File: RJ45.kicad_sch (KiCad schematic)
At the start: 13 parts, among them J1 0826-1X1T-JK-F, U1 KSZ8081MLX, U8 OSC_25M

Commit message: Routing changes, pullups, etc
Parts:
- C1, C2, C3, C34, C35, C36, C4, J1, R1, R23, R24, U1: Source (none) -> ANY
- U8: value OSC_25M -> ASEMB-25.000MHZ-LC-T; Source (none) -> ANY

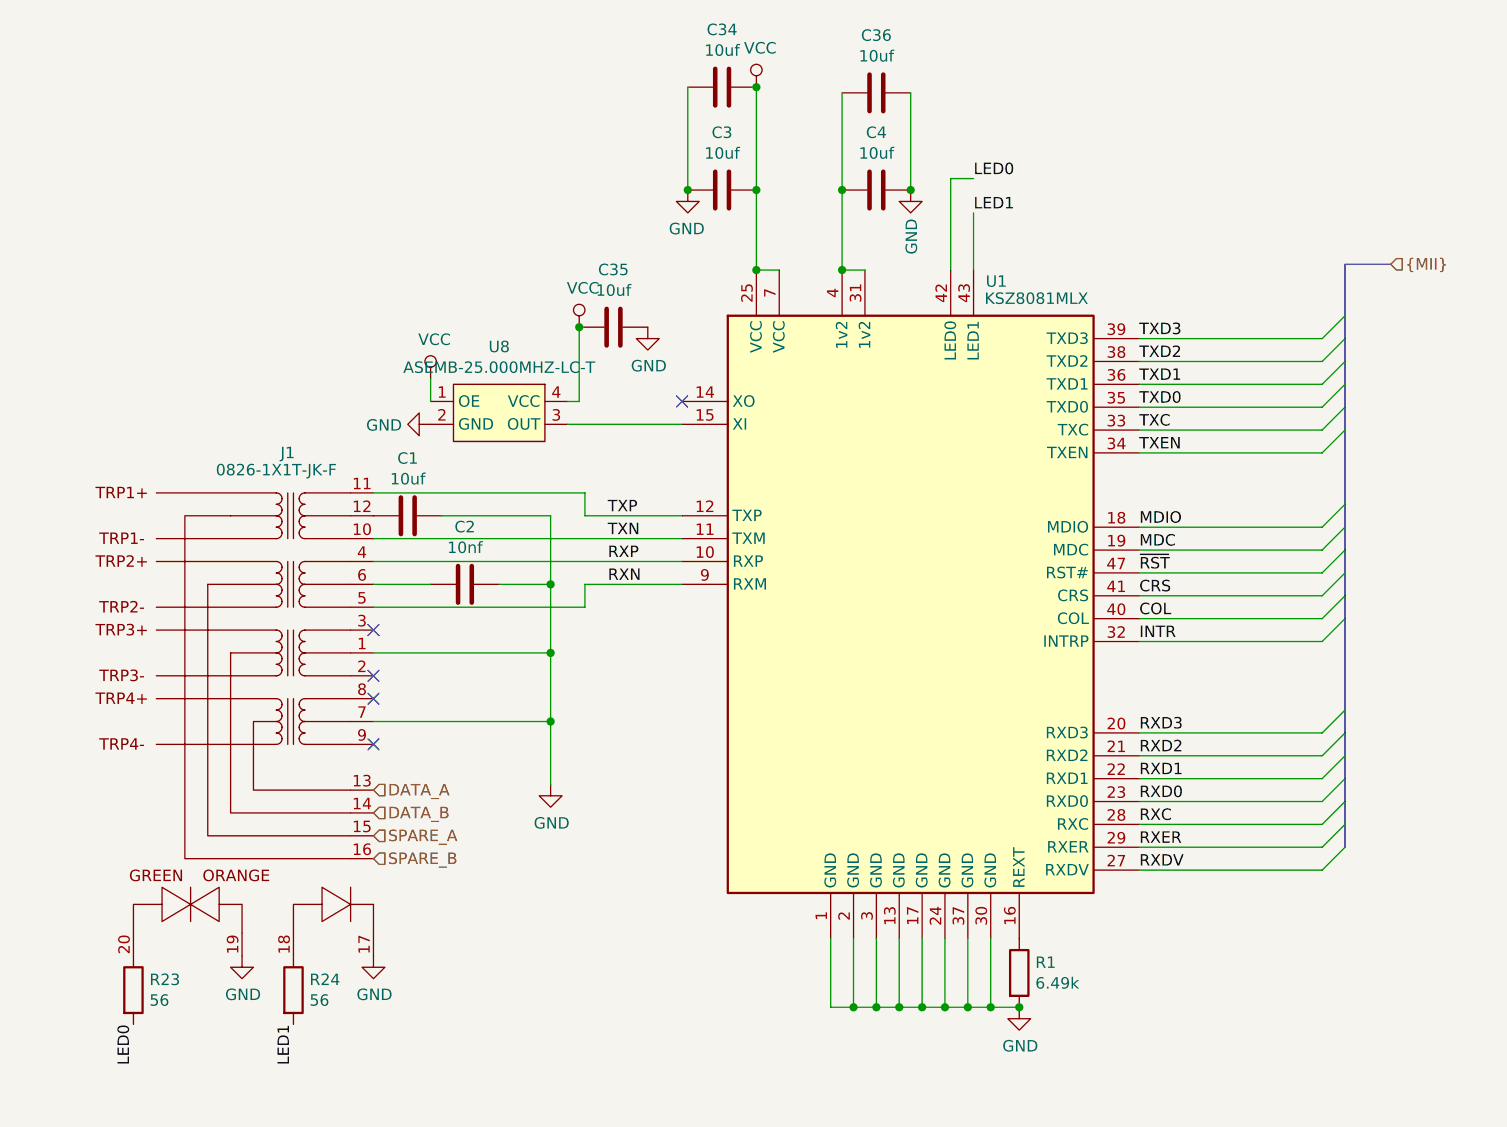
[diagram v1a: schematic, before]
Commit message: Routing cleanup, fix primary transformer
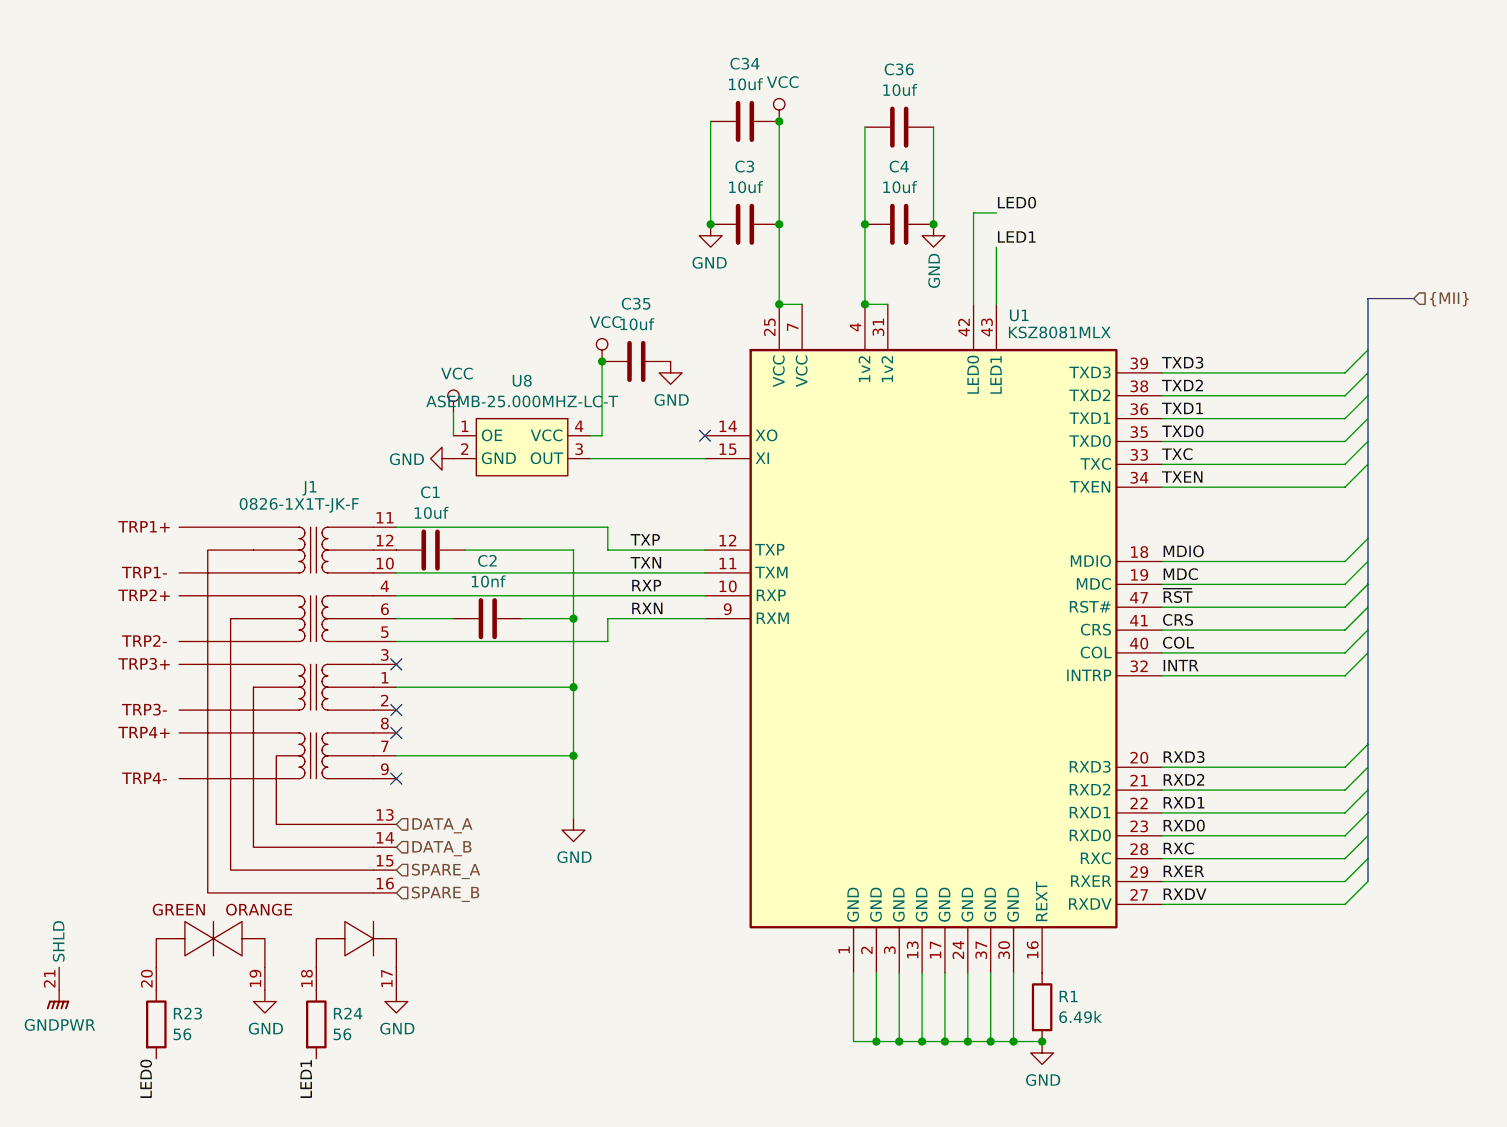
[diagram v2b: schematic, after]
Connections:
- new net GNDPWR: J1.21 (SHLD), J1.22 (SHLD)
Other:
- moved on the sheet: C1, C2, C3, C34, C35, C36, C4, R1, R23, R24, U1, U8

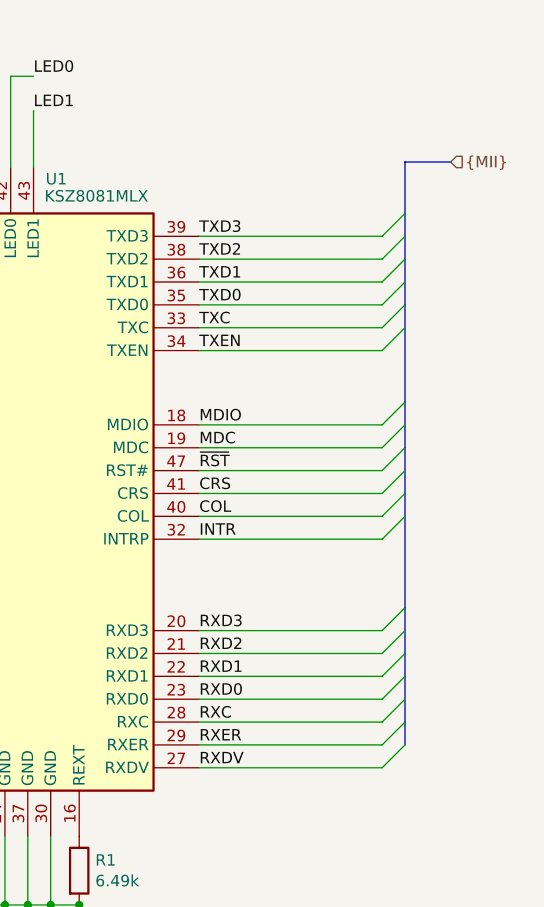
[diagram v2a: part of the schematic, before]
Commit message: Change PoE controller to NCP1081
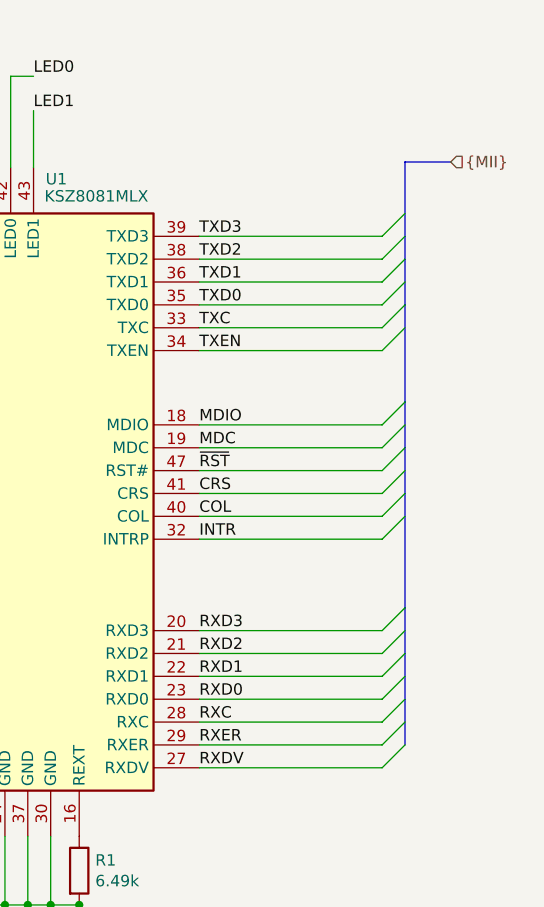
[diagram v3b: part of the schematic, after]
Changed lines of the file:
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@@
-(kicad_sch (version 20200512) (host eeschema "5.99.0-unknown-eae0c14~101~ubuntu20.04.1")
+(kicad_sch (version 20200608) (host eeschema "5.99.0-unknown-8bd9b26~101~ubuntu20.04.1")
   (page 2 7)
   (paper "A4")
@@
   (junction (at 177.8 137.795))
   (junction (at 180.975 137.795))
-  (no_connect (at 109.22 95.885))
   (no_connect (at 109.22 103.505))
   (no_connect (at 109.22 100.965))
+  (no_connect (at 109.22 108.585))
   (no_connect (at 143.51 70.485))
-  (no_connect (at 109.22 108.585))
+  (no_connect (at 109.22 95.885))
   (bus_entry (at 214.63 63.5) (size 2.54 -2.54))
   (bus_entry (at 214.63 66.04) (size 2.54 -2.54))
@@
     (stroke (width 0) (type solid) (color 0 0 0 0))
   )
-  (bus (pts (xy 217.17 55.245) (xy 217.17 60.96))
+  (bus (pts (xy 217.17 55.245) (xy 217.17 63.5))
     (stroke (width 0) (type solid) (color 0 0 0 0))
   )
@@
     (stroke (width 0) (type solid) (color 0 0 0 0))
   )
-  (bus (pts (xy 217.17 60.96) (xy 217.17 66.04))
+  (bus (pts (xy 217.17 63.5) (xy 217.17 66.04))
     (stroke (width 0) (type solid) (color 0 0 0 0))
   )
@@
     (stroke (width 0) (type solid) (color 0 0 0 0))
   )
-  (bus (pts (xy 217.17 109.855) (xy 217.17 112.395))
-    (stroke (width 0) (type solid) (color 0 0 0 0))
-  )
-  (bus (pts (xy 217.17 112.395) (xy 217.17 117.475))
-    (stroke (width 0) (type solid) (color 0 0 0 0))
-  )
-  (bus (pts (xy 217.17 117.475) (xy 217.17 120.015))
+  (bus (pts (xy 217.17 109.855) (xy 217.17 114.935))
+    (stroke (width 0) (type solid) (color 0 0 0 0))
+  )
+  (bus (pts (xy 217.17 114.935) (xy 217.17 120.015))
     (stroke (width 0) (type solid) (color 0 0 0 0))
   )
@@
   )
   (symbol (lib_id "power:VCC") (at 115.57 67.945 0) (unit 1)
+    (in_bom yes) (on_board yes)
     (property "Reference" "#PWR0170" (id 0) (at 115.57 71.755 0)
       (effects (font (size 1.27 1.27)) hide)
@@
   )
   (symbol (lib_id "power:VCC") (at 132.08 62.23 0) (unit 1)
+    (in_bom yes) (on_board yes)
     (property "Reference" "#PWR0171" (id 0) (at 132.08 66.04 0)
       (effects (font (size 1.27 1.27)) hide)
@@
   )
   (symbol (lib_id "power:VCC") (at 151.765 35.56 0) (unit 1)
+    (in_bom yes) (on_board yes)
     (property "Reference" "#PWR0102" (id 0) (at 151.765 39.37 0)
       (effects (font (size 1.27 1.27)) hide)
@@
   )
   (symbol (lib_id "power:GNDPWR") (at 71.755 132.08 0) (unit 1)
+    (in_bom yes) (on_board yes)
     (property "Reference" "#PWR0182" (id 0) (at 71.755 137.16 0)
       (effects (font (size 1.27 1.27)) hide)
@@
   )
   (symbol (lib_id "power:GND") (at 94.615 132.08 0) (unit 1)
+    (in_bom yes) (on_board yes)
     (property "Reference" "#PWR0175" (id 0) (at 94.615 138.43 0)
       (effects (font (size 1.27 1.27)) hide)
@@
   )
   (symbol (lib_id "power:GND") (at 109.22 132.08 0) (unit 1)
+    (in_bom yes) (on_board yes)
     (property "Reference" "#PWR0174" (id 0) (at 109.22 138.43 0)
       (effects (font (size 1.27 1.27)) hide)
@@
   )
   (symbol (lib_id "power:GND") (at 115.57 73.025 270) (unit 1)
+    (in_bom yes) (on_board yes)
     (property "Reference" "#PWR0172" (id 0) (at 109.22 73.025 0)
       (effects (font (size 1.27 1.27)) hide)
@@
   )
   (symbol (lib_id "power:GND") (at 128.905 113.03 0) (unit 1)
+    (in_bom yes) (on_board yes)
     (property "Reference" "#PWR0105" (id 0) (at 128.905 119.38 0)
       (effects (font (size 1.27 1.27)) hide)
@@
   )
   (symbol (lib_id "power:GND") (at 139.7 62.23 0) (unit 1)
+    (in_bom yes) (on_board yes)
     (property "Reference" "#PWR0173" (id 0) (at 139.7 68.58 0)
       (effects (font (size 1.27 1.27)) hide)
@@
   )
   (symbol (lib_id "power:GND") (at 144.145 46.99 0) (mirror y) (unit 1)
+    (in_bom yes) (on_board yes)
     (property "Reference" "#PWR0103" (id 0) (at 144.145 53.34 0)
       (effects (font (size 1.27 1.27)) hide)
@@
   )
   (symbol (lib_id "power:GND") (at 168.91 46.99 0) (unit 1)
+    (in_bom yes) (on_board yes)
     (property "Reference" "#PWR0104" (id 0) (at 168.91 53.34 0)
       (effects (font (size 1.27 1.27)) hide)
@@
   )
   (symbol (lib_id "power:GND") (at 180.975 137.795 0) (unit 1)
+    (in_bom yes) (on_board yes)
     (property "Reference" "#PWR0101" (id 0) (at 180.975 144.145 0)
       (effects (font (size 1.27 1.27)) hide)
@@
   )
   (symbol (lib_name "Device:R_1") (lib_id "Device:R") (at 82.55 135.89 0) (unit 1)
+    (in_bom yes) (on_board yes)
     (property "Reference" "R23" (id 0) (at 84.3281 134.7406 0)
       (effects (font (size 1.27 1.27)) (justify left))
@@
   )
   (symbol (lib_name "Device:R_2") (lib_id "Device:R") (at 100.33 135.89 0) (unit 1)
+    (in_bom yes) (on_board yes)
     (property "Reference" "R24" (id 0) (at 102.1081 134.7406 0)
       (effects (font (size 1.27 1.27)) (justify left))
@@
   )
   (symbol (lib_id "Device:R") (at 180.975 133.985 0) (unit 1)
+    (in_bom yes) (on_board yes)
     (property "Reference" "R1" (id 0) (at 182.7531 132.8356 0)
       (effects (font (size 1.27 1.27)) (justify left))
@@
   )
   (symbol (lib_id "Device:C") (at 113.03 83.185 90) (unit 1)
+    (in_bom yes) (on_board yes)
     (property "Reference" "C1" (id 0) (at 113.03 76.8158 90))
     (property "Value" "10uf" (id 1) (at 113.03 79.1145 90))
@@
   )
   (symbol (lib_name "Device:C_2") (lib_id "Device:C") (at 119.38 90.805 90) (unit 1)
+    (in_bom yes) (on_board yes)
     (property "Reference" "C2" (id 0) (at 119.38 84.4358 90))
     (property "Value" "10nf" (id 1) (at 119.38 86.7345 90))
@@
   )
   (symbol (lib_name "Device:C_1") (lib_id "Device:C") (at 135.89 62.23 90) (unit 1)
+    (in_bom yes) (on_board yes)
     (property "Reference" "C35" (id 0) (at 135.89 55.8608 90))
     (property "Value" "10uf" (id 1) (at 135.89 58.1595 90))
@@
   )
   (symbol (lib_name "Device:C_4") (lib_id "Device:C") (at 147.955 35.56 270) (mirror x) (unit 1)
+    (in_bom yes) (on_board yes)
     (property "Reference" "C34" (id 0) (at 147.955 29.1908 90))
     (property "Value" "10uf" (id 1) (at 147.955 31.4895 90))
@@
   )
   (symbol (lib_name "Device:C_3") (lib_id "Device:C") (at 147.955 46.99 270) (mirror x) (unit 1)
+    (in_bom yes) (on_board yes)
     (property "Reference" "C3" (id 0) (at 147.955 40.6208 90))
     (property "Value" "10uf" (id 1) (at 147.955 42.9195 90))
@@
   )
   (symbol (lib_name "Device:C_5") (lib_id "Device:C") (at 165.1 36.195 90) (unit 1)
+    (in_bom yes) (on_board yes)
     (property "Reference" "C36" (id 0) (at 165.1 29.8258 90))
     (property "Value" "10uf" (id 1) (at 165.1 32.1245 90))
@@
   )
   (symbol (lib_name "Device:C_6") (lib_id "Device:C") (at 165.1 46.99 90) (unit 1)
+    (in_bom yes) (on_board yes)
     (property "Reference" "C4" (id 0) (at 165.1 40.6208 90))
     (property "Value" "10uf" (id 1) (at 165.1 42.9195 90))
@@
   )
   (symbol (lib_id "h75_poe:OSC_25M") (at 123.19 68.58 0) (unit 1)
+    (in_bom yes) (on_board yes)
     (property "Reference" "U8" (id 0) (at 123.19 64.4208 0))
     (property "Value" "ASEMB-25.000MHZ-LC-T" (id 1) (at 123.19 66.7195 0))
@@
   )
   (symbol (lib_id "h75_poe:0826-1X1T-JK-F") (at 97.155 94.615 0) (mirror y) (unit 1)
+    (in_bom yes) (on_board yes)
     (property "Reference" "J1" (id 0) (at 99.695 76.2 0))
     (property "Value" "0826-1X1T-JK-F" (id 1) (at 98.425 78.105 0))
@@
   )
   (symbol (lib_id "h75_poe:KSZ8081MLX") (at 168.91 93.98 0) (unit 1)
+    (in_bom yes) (on_board yes)
     (property "Reference" "U1" (id 0) (at 178.435 57.15 0))
     (property "Value" "KSZ8081MLX" (id 1) (at 182.88 59.055 0))
